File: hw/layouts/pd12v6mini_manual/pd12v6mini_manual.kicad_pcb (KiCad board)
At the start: 4 copper layers, 33 x 20 mm, 28 parts

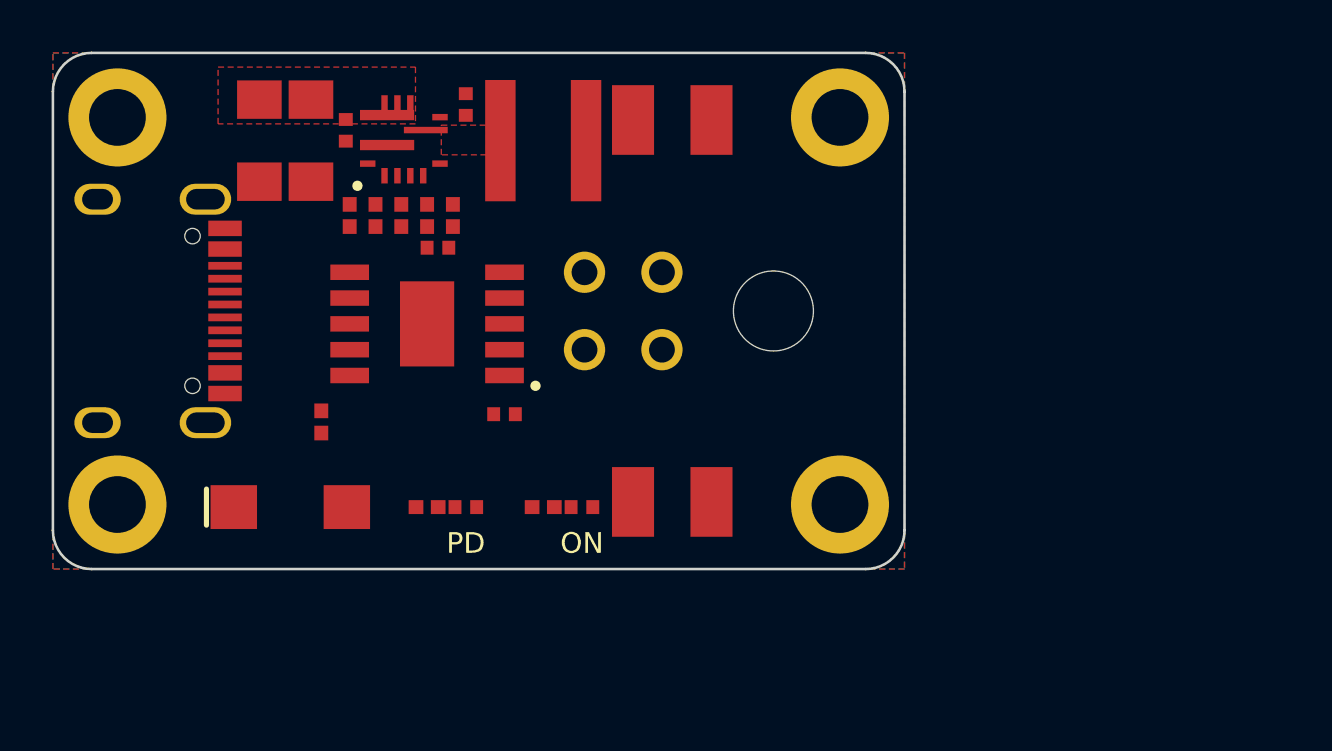
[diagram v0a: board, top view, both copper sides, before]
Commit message: pd12v6mini rev B: grouped hand layout, every part labelled, consistent routing
- 35x24.5 mm: INPUT left, BUCK along the top with a 2 mm-pitch control row,
  PD controller centred with mirrored PD/ON status columns, output caps
  mirrored about the Micro-Fit. White inset outline restored, holes inset.
- Routing redone: one width per job (0.2 sig / 0.3 tap / 0.6 power), straight
  pad exits, uniform 45-degree chamfers, top layer pad-to-pad only (USB data
  on B.Cu, CC2 on In2, power via In2 pours). DRC clean, 0 unconnected.

Co-Authored-By: Claude Opus 5.5 <noreply@anthropic.com>
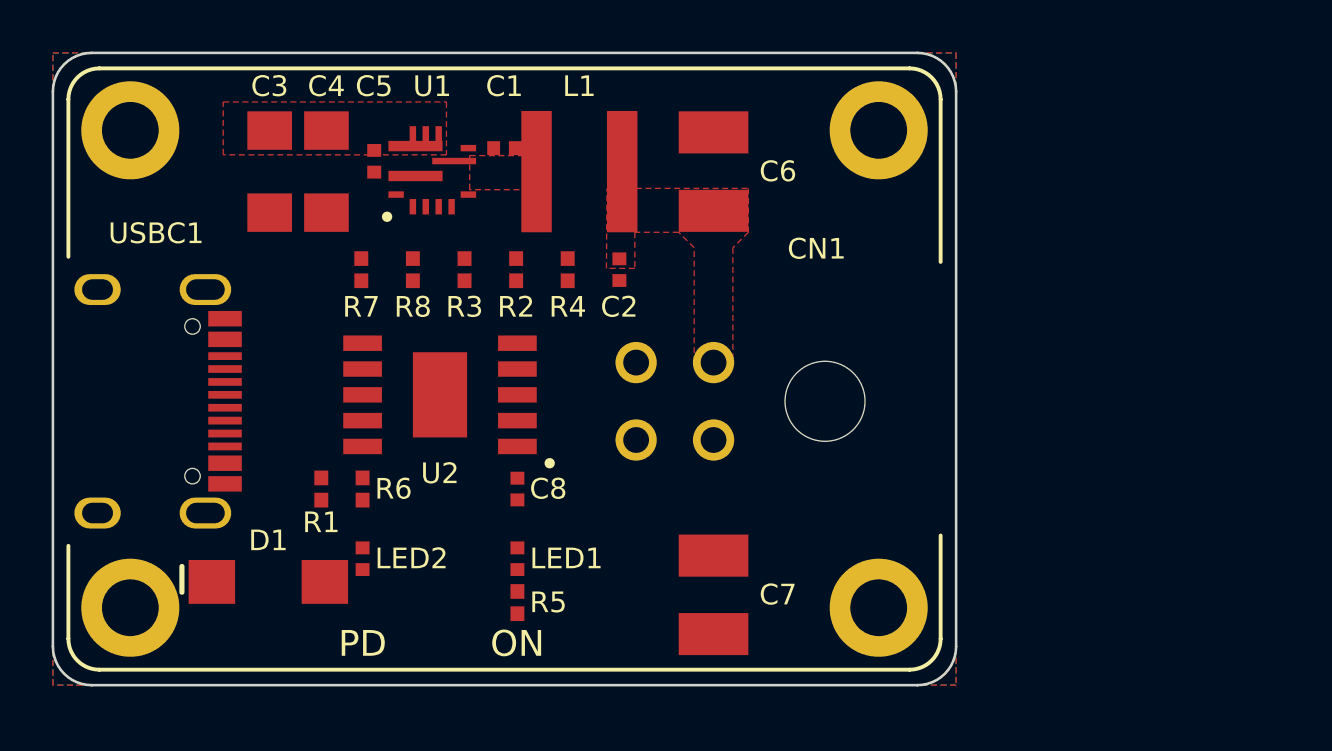
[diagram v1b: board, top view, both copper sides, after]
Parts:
- moved C2 7.08 mm to (21.9, 8.40), turned to -90 degrees
- moved R4 5.84 mm to (19.9, 8.40)
- moved LED2 4.47 mm to (12.0, 19.6), turned to -90 degrees
- moved H4 4.27 mm to (32.0, 21.5)
- moved CN1 4.03 mm to (24.1, 13.5)
- moved H3 4.03 mm to (3.00, 21.5)
- moved C7 3.94 mm to (25.6, 21.0), turned to 90 degrees
- moved R5 3.83 mm to (18.0, 21.3), turned to -90 degrees
- moved USBC1 3.50 mm to (4.20, 13.5)
- moved R2 3.23 mm to (17.9, 8.40)
- moved R3 3.23 mm to (15.9, 8.40)
- moved LED1 3.20 mm to (18.0, 19.6), turned to 90 degrees
- moved D1 3.02 mm to (8.35, 20.5)
- moved C8 2.94 mm to (18.0, 16.9), turned to -90 degrees
- moved U2 2.80 mm to (15.0, 13.2)
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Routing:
- added copper zone on F.Cu, net VOUT
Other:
- board size 33 x 20 mm -> 35 x 24.5 mm
- board text added: "rev B 2026-10"
- board text removed: "rev A 2026-10"

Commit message: pd12v6mini rev E: 6.8 uH 12.5 A inductor, third input cap, 47.5 x 25 mm
TI WEBENCH (real TPS56637 model) flagged the 5.6 uH / 8.6 A Isat inductor (overload peak
~10 A) and ~8 uF effective input capacitance. Rev E uses PROD PSTMAA666460-6R8MB (C55172548)
and adds C9 (10 uF 1206, Basic). Re-sim: settling 0.14 ms, 1.6 W lost at 20 V / 5 A.

- revs B, C, D kept in hw/layouts/pd12v6mini_revX
- CC2 rerouted clear of the back text; VOUT strip clear of the CN1 label
- ngspice buck and UVLO decks in hw/sim
- scripts/fab_export.sh: JLCPCB gerber zip, BOM and CPL from the stored fill
- docs/pd12v6/mini.md: WEBENCH results, JLCPCB quote so far, DIY parts cost

Co-Authored-By: Claude Opus 5.5 <noreply@anthropic.com>
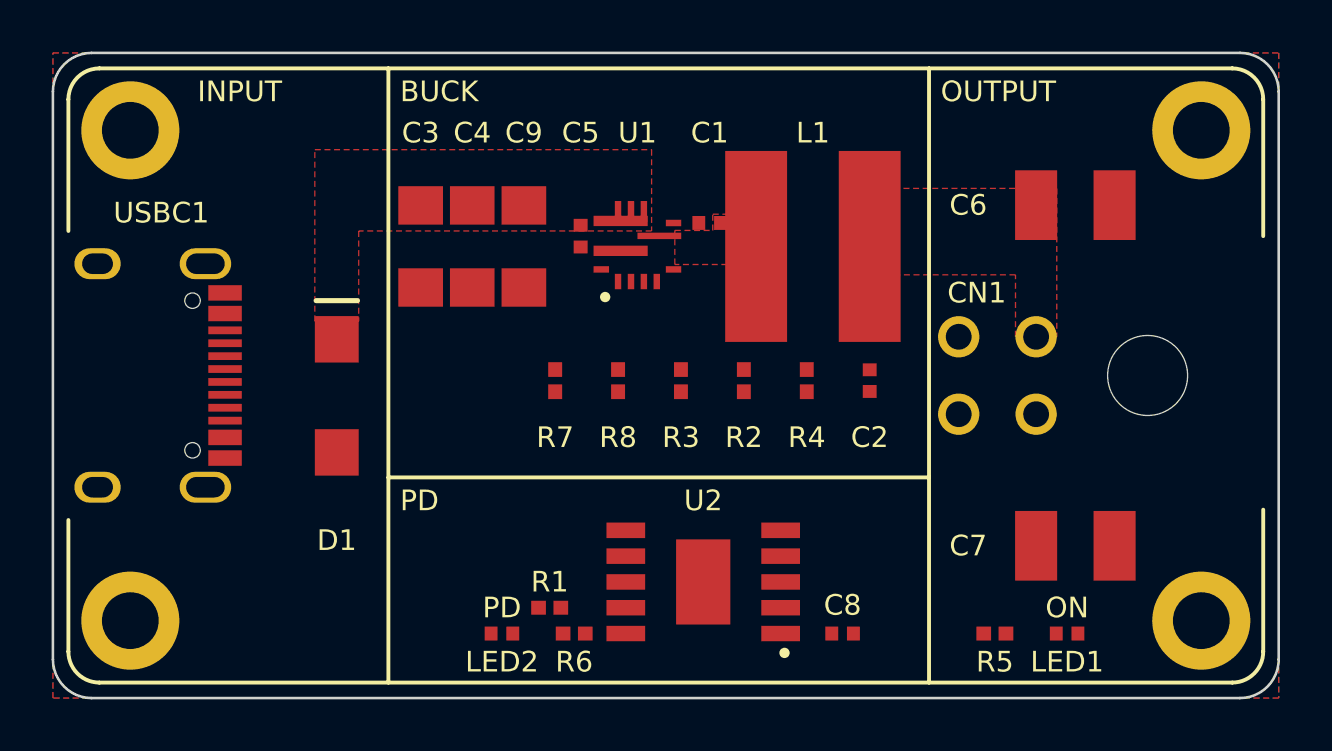
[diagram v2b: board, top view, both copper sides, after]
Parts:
- added C9: , SAMSUNG_CL31A106KBHNNNE:C1206, F.Cu at (18.2, 7.50)
- L1: footprint YJYCOIN_YSPIT0550A_5R6M:IND-SMD_L5.5-W5.3 -> PROD_PSTMAA666460_6R8MB:IND-SMD_PSTMAA666460-6R8MB
- R8: footprint UNI_ROYAL_0402WGF2702TCE:R0402 -> UNI_ROYAL_0402WGF3002TCE:R0402
- moved LED1 21.5 mm to (39.3, 22.5), turned to 0 degrees
- moved R5 18.5 mm to (36.5, 22.5), turned to 180 degrees
- moved C7 14.1 mm to (39.6, 19.1), turned to 180 degrees
- moved C6 14.1 mm to (39.6, 5.90), turned to 0 degrees
- moved C8 13.8 mm to (30.6, 22.5), turned to 0 degrees
- moved CN1 12.5 mm to (36.6, 12.5)
- moved U2 12.5 mm to (25.2, 20.5)
- moved H4 12.5 mm to (44.5, 22.0)
- moved H2 12.5 mm to (44.5, 3.00)
- moved C2 10.6 mm to (31.6, 12.7)
- moved R4 10.2 mm to (29.2, 12.7)
- moved R1 9.97 mm to (19.2, 21.5), turned to 180 degrees
- moved R6 9.93 mm to (20.2, 22.5), turned to 0 degrees
- moved R2 9.82 mm to (26.8, 12.7)
- moved L1 9.50 mm to (29.4, 7.50)
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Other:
- board size 35 x 24.5 mm -> 47.5 x 25 mm
- board text added: "BUCK"
- board text added: "INPUT"
- board text added: "OUTPUT"
- board text added: "rev E 2026-10"
- board text removed: "rev B 2026-10"
